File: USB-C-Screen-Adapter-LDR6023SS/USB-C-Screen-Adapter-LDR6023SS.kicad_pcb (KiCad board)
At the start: 2 copper layers, 50 x 50 mm, 42 parts, among them J1 USB_C_Receptacle, J2 USB, SW1 BRIGHTNESS, U2 5022505191, U3 LDR6023SS, U4 USBLC6-4, U5 SY7200AABC, U6 SY7200AABC, U7 AMS1117-3.3

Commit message: updated schematic
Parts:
- moved J2 165.6 mm to (101.8, 121.4)
- moved R3 158.7 mm to (149.3, 122.5)
- moved C7 155.2 mm to (117.2, 124.6), turned to 270 degrees
- moved C8 153.5 mm to (118.0, 124.6), turned to 270 degrees
- moved U7 144.6 mm to (104.8, 114.0), turned to 90 degrees
- moved H1 141.2 mm to (127.5, 103.5)
- moved C6 139.8 mm to (113.1, 114.2), turned to 270 degrees
- moved C5 137.6 mm to (112.1, 114.2), turned to 270 degrees
- moved J1 132.9 mm to (115.5, 130.0)
- moved U3 131.1 mm to (107.2, 123.8)
- moved H2 127.4 mm to (103.5, 103.5)
- moved U2 124.0 mm to (115.5, 103.6)
- moved C10 99.1 mm to (117.0, 69.7)
- moved C12 99.1 mm to (98.6, 88.5)
- moved C14 99.1 mm to (116.9, 66.7)
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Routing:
- net L3_N: track 0.00 -> 25.5 mm, vias 0 -> 2
- net L3_P: track 0.00 -> 23.3 mm
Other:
- board size 50 x 50 mm -> 31 x 34.3 mm
- net class Default: trace_width 0.25 -> 0.2; via_dia 0.8 -> 0.6; via_drill 0.4 -> 0.3
- rule pad_to_mask_clearance: 0.051 -> 0
- rule trace_min: 0.2 -> 0.15

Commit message: updated schematic
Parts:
- moved SW1 66.5 mm to (125.5, 128.5)
- moved R3 55.1 mm to (95.9, 108.8)
- moved C5 5.36 mm to (112.4, 108.9)
- moved C6 5.35 mm to (113.2, 108.9)
- moved U7 1.92 mm to (105.2, 112.1)
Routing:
- net AUX_P: track 0.00 -> 33.1 mm, vias 0 -> 4
- net AUX_N: track 0.00 -> 29.0 mm, vias 0 -> 2
- net L2_P: track 0.00 -> 28.6 mm, vias 0 -> 2
- net L2_N: track 0.00 -> 28.4 mm, vias 0 -> 2
- net /_L1_P: track 0.00 -> 23.1 mm, vias 0 -> 2
- net /_L1_N: track 0.00 -> 22.7 mm, vias 0 -> 2
- net L0_N: track 0.00 -> 22.2 mm, vias 0 -> 2
- net L0_P: track 0.00 -> 22.2 mm, vias 0 -> 2
- net CC2: track 0.00 -> 12.7 mm
- net CC1: track 0.00 -> 12.7 mm, vias 0 -> 2
- net USB_N: track 0.00 -> 5.98 mm, vias 0 -> 2
- net L1_P: track 0.00 -> 3.64 mm
- net L1_N: track 0.00 -> 3.64 mm
- net +5V: track 0.00 -> 2.86 mm, vias 0 -> 4
- net /_L0_N: track 0.00 -> 2.33 mm
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- added copper zone on B.Cu, net +5V
- added copper zone on F.Cu, net +5V
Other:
- net class Default: clearance 0.2 -> 0.157
- rule trace_clearance: 0.2 -> 0.157

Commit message: updated layout
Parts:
- moved R2 77.2 mm to (130.2, 129.0), turned to 90 degrees
- moved R1 72.4 mm to (121.0, 128.5), turned to 270 degrees
- moved U4 68.5 mm to (107.5, 130.8), turned to 90 degrees
- moved R9 61.8 mm to (129.5, 110.0), turned to 90 degrees
- moved R8 59.0 mm to (124.2, 110.0), turned to 90 degrees
- moved C14 55.5 mm to (121.8, 122.0)
- moved C13 54.0 mm to (127.2, 122.0)
- moved L1 53.5 mm to (122.4, 118.9)
- moved C15 52.9 mm to (127.2, 123.8)
- moved D4 49.1 mm to (127.8, 115.5)
- moved D3 48.9 mm to (122.4, 115.5)
- moved L2 48.6 mm to (127.8, 118.9)
- moved R5 44.9 mm to (104.9, 128.4), turned to 180 degrees
- moved U6 43.3 mm to (128.0, 112.6), turned to 180 degrees
- moved R4 43.2 mm to (103.8, 119.1)
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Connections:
- SW1 pad 1: LEDC1DIM -> LEDC2DIM
- SW1 pad 4: LEDC2DIM -> LEDC1DIM
- U3 pad 5: Net-(U3-Pad10) -> Net-(U3-Pad5)
- U3 pad 6: Net-(U3-Pad10) -> Net-(U3-Pad6)
- U3 pad 9: Net-(U3-Pad10) -> Net-(U3-Pad9)
- U4 pad 1: USB_N -> USB_P
- U4 pad 6: USB_P -> USB_N
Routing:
- net +5V: track 2.86 -> 75.6 mm, vias 4 -> 13
- net USB_P: track 1.43 -> 36.7 mm, vias 0 -> 2
- net GND: track 0.00 -> 28.6 mm, vias 0 -> 101
- net LEDC1: track 0.00 -> 27.3 mm, vias 0 -> 2
- net USB_N: track 5.98 -> 31.6 mm, vias 2 -> 3
- net LEDC2DIM: track 0.00 -> 24.1 mm, vias 0 -> 2
- net LEDC2: track 0.00 -> 24.0 mm, vias 0 -> 2
- net +3V3: track 0.00 -> 20.4 mm
- net LEDC1DIM: track 0.00 -> 19.8 mm, vias 0 -> 2
- net Net-(R4-Pad1): track 0.00 -> 9.25 mm, vias 0 -> 2
- net LEDA1: track 0.00 -> 9.04 mm
- net PWM: track 0.00 -> 7.10 mm, vias 0 -> 2
- net Net-(C4-Pad1): track 0.00 -> 6.57 mm
- net LEDA2: track 0.00 -> 6.38 mm
- net AUX_N: track 29.0 -> 33.2 mm
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- added copper zone on F.Cu, net +3V3
- added copper zone on B.Cu, net GND
- added copper zone on F.Cu, net GND
- added copper zone on F.Cu, net LEDA1
- added copper zone on F.Cu, net LEDA2
- added copper zone on F.Cu, net Net-(D3-Pad2)
- added copper zone on F.Cu, net Net-(D4-Pad2)

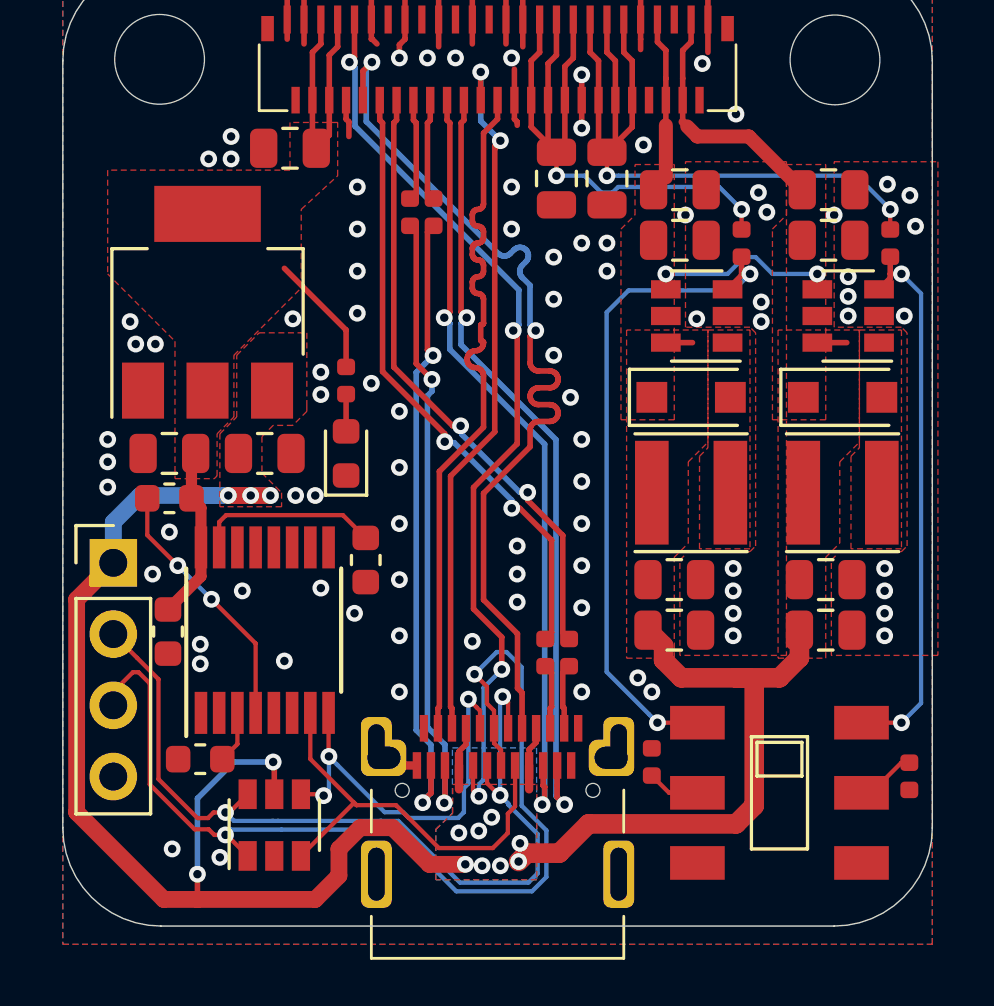
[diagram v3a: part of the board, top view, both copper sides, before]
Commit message: updated layout
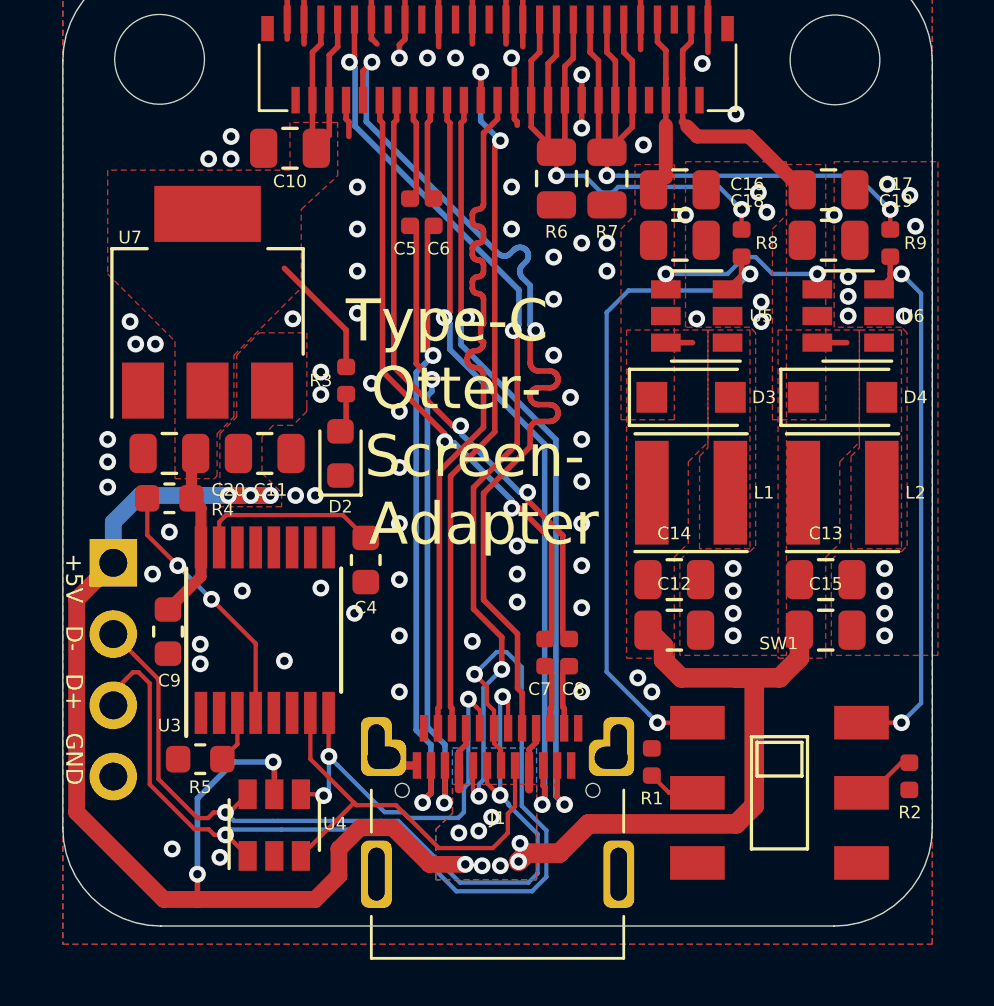
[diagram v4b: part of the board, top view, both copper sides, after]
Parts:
- moved D2 0.20 mm to (109.9, 117.5)
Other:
- board text added: "+5V D- D+ GND"
- board text added: "Type-C Otter- Screen- Adapter"

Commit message: fixed otter-screen-adapter, added gerber
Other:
- board text added: "Design by Jan Henrik Hemsing 2019"
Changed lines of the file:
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@@
   (general
     (thickness 1.6)
-    (drawings 10)
+    (drawings 11)
     (tracks 840)
     (zones 0)
@@
     (35 F.Paste user)
     (36 B.SilkS user)
-    (37 F.SilkS user)
+    (37 F.SilkS user hide)
     (38 B.Mask user)
     (39 F.Mask user)
@@
   )
   (setup
-    (last_trace_width 0.3)
+    (last_trace_width 0.2)
     (user_trace_width 0.154)
     (user_trace_width 0.2)
@@
     (pcbplotparams
       (layerselection 0x010fc_ffffffff)
-      (usegerberextensions false)
+      (usegerberextensions true)
       (usegerberattributes false)
       (usegerberadvancedattributes false)
@@
       (outputformat 1)
       (mirror false)
-      (drillshape 1)
+      (drillshape 0)
       (scaleselection 1)
-      (outputdirectory ""))
+      (outputdirectory "gerber/"))
   )
   (net 0 "")
@@
   (module otter:K3-2235S-K1 (layer F.Cu)
     (at 125.55 129.6)
-    (fp_text reference SW1 (at -0.025 -5.325) (layer F.SilkS)
+    (fp_text reference SW1 (at -0.025 -2.5) (layer F.SilkS)
       (effects (font (size 0.45 0.45) (thickness 0.1)))
     )
@@
     (tags capacitor)
     (attr smd)
-    (fp_text reference C15 (at 0 -1.65) (layer F.SilkS)
+    (fp_text reference C15 (at 0 1.9) (layer F.SilkS)
       (effects (font (size 0.45 0.45) (thickness 0.1)))
     )
@@
     (tags capacitor)
     (attr smd)
-    (fp_text reference C14 (at 0 -1.65) (layer F.SilkS)
+    (fp_text reference C14 (at 0 3.1) (layer F.SilkS)
       (effects (font (size 0.45 0.45) (thickness 0.1)))
     )
@@
     (tags capacitor)
     (attr smd)
-    (fp_text reference C13 (at 0 -1.65) (layer F.SilkS)
+    (fp_text reference C13 (at 0 3.1) (layer F.SilkS)
       (effects (font (size 0.45 0.45) (thickness 0.1)))
     )
@@
     (tags capacitor)
     (attr smd)
-    (fp_text reference C12 (at 0 -1.65) (layer F.SilkS)
+    (fp_text reference C12 (at 0 1.9) (layer F.SilkS)
       (effects (font (size 0.45 0.45) (thickness 0.1)))
     )
@@
       (rotate (xyz 0 0 0))
     )
+  )
+  (gr_text "Design by\nJan Henrik Hemsing\n2019" (at 125.1 132.5) (layer B.SilkS)
+    (effects (font (size 0.5 0.5) (thickness 0.1)) (justify mirror))
   )
   (gr_text "+5V   D-   D+   GND" (at 100.4 125.2 270) (layer F.SilkS)
@@
     (min_thickness 0.1)
     (keepout (tracks allowed) (vias allowed) (copperpour not_allowed))
-    (fill (arc_segments 32) (thermal_gap 0.2) (thermal_bridge_width 0.8) (smoothing chamfer) (radius 0.1))
+    (fill (arc_segments 32) (thermal_gap 0.2) (thermal_bridge_width 0.8))
     (polygon
       (pts
